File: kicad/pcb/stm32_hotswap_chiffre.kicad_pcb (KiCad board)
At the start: 2 copper layers, 227.4 x 84.9 mm, 119 parts, among them J1 USB_C_Receptacle_USB2.0, J2 SAM, J3 nRF52, J4 Conn_01x02_Socket, J5 Conn_01x02_Socket, Q2 AO3401A, SW1 SW_Push, SW10 SW_Push, SW11 SW_Push, SW12 SW_Push, SW13 SW_Push, SW14 SW_Push, SW15 SW_Push, SW16 SW_Push, SW17 SW_Push, SW18 SW_Push, SW19 SW_Push, SW2 SW_Push, SW20 SW_Push, SW21 SW_Push, SW22 SW_Push, SW23 SW_Push, SW24 SW_Push, SW25 SW_Push, SW26 SW_Push, SW27 SW_Push, SW28 SW_Push, SW29 SW_Push, SW3 SW_Push, SW30 SW_Push, SW31 SW_Push, SW32 SW_Push, SW33 SW_Push, SW34 SW_Push, SW35 SW_Push, SW37 Reset, SW4 SW_Push, SW5 SW_Push, SW6 SW_Push, SW7 SW_Push, SW8 SW_Push, SW9 SW_Push, U2 PRTR5V0U2X, U3 XC6206PxxxMR-Regulator_Linear, U4 ATSAML21E18B-AUT, U5 BC805M, U6 MCP73832-2-OT, U7 74LVC1G08, U8 74LVC1G08, U9 74LVC1G08, Y2 32.768 kHz

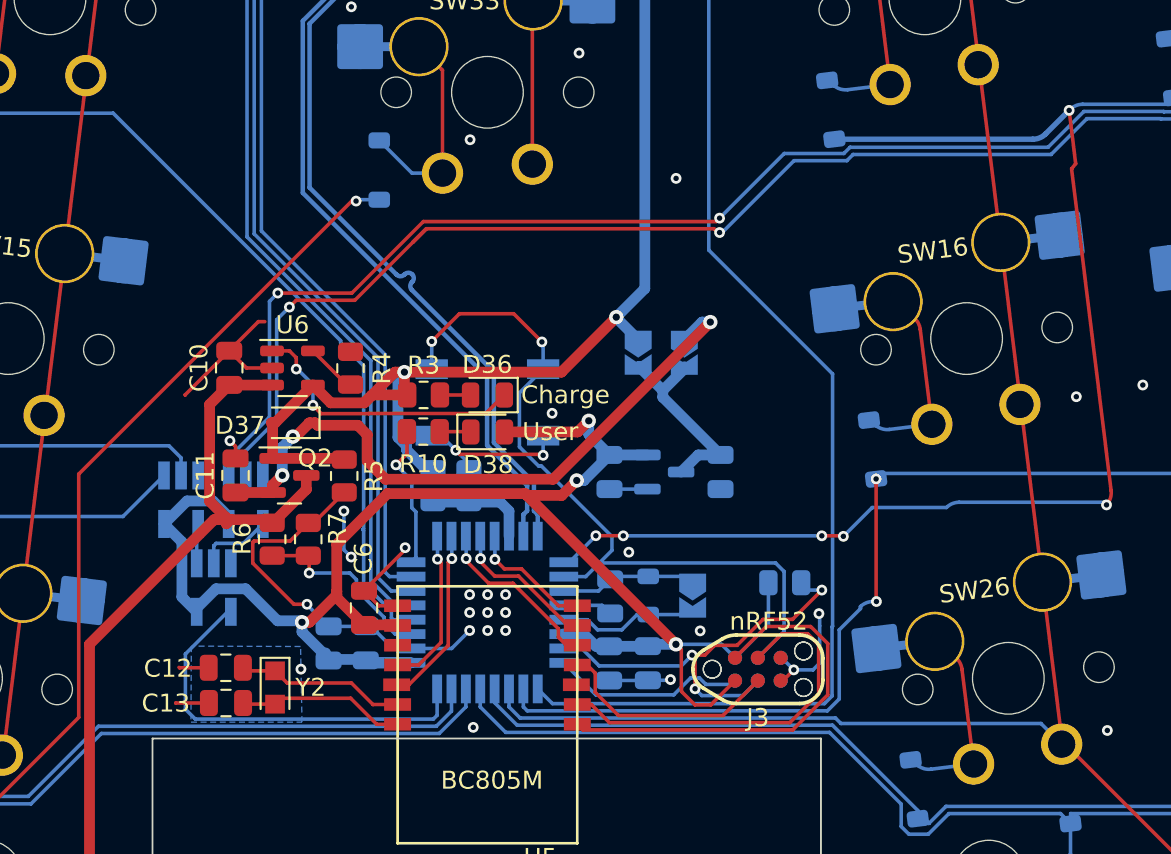
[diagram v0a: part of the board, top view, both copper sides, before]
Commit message: Rework pins to use proper wake/interrupt pins for all matrix outputs, fix edge cuts.
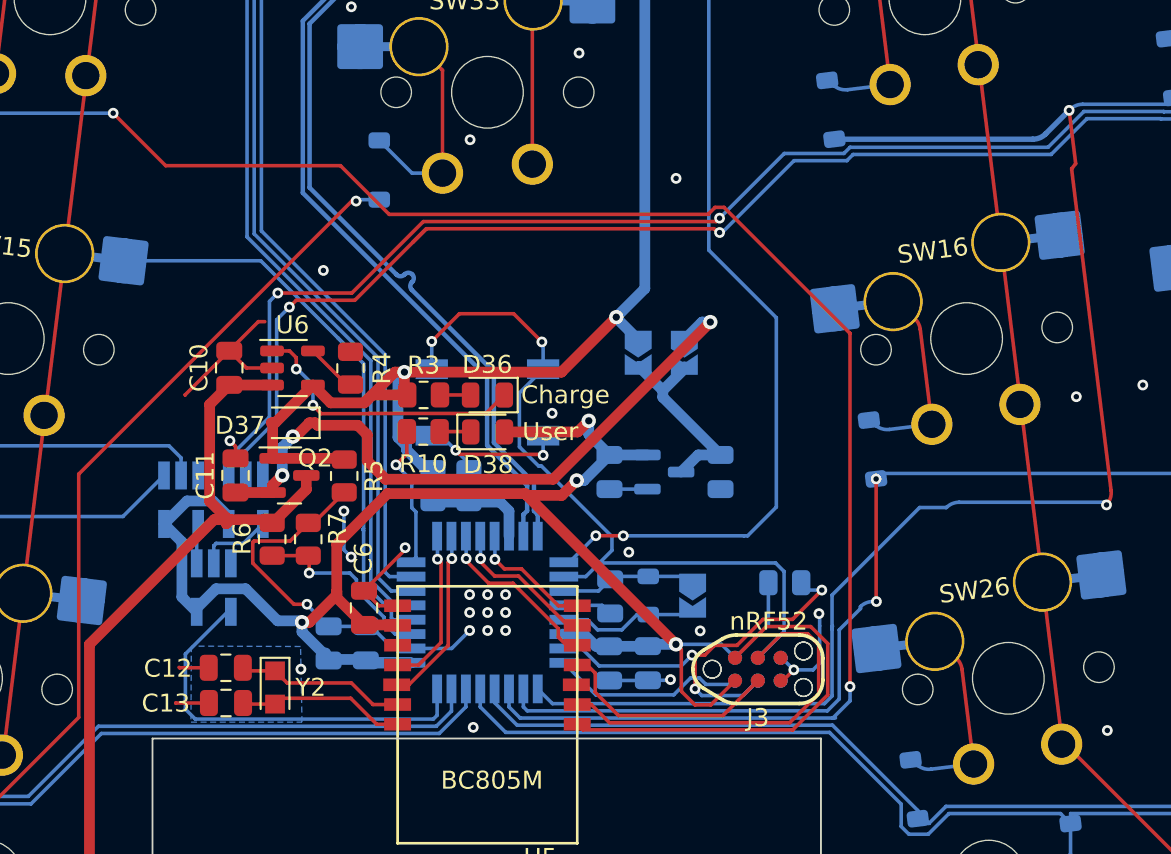
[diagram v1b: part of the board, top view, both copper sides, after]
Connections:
- U4 pad 1: col0 -> row0_r
- U4 pad 12: row0_l -> col4
- U4 pad 25: row0_r -> col0
- U4 pad 3: col4 -> row0_l
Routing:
- net row0_l: track 128.9 -> 180.8 mm, vias 0 -> 2
- net col0: track 425.5 -> 409.6 mm, vias 1 -> 3
- net row0_r: track 136.1 -> 144.9 mm, vias 6 -> 2
- net -BATT: vias 101 -> 102

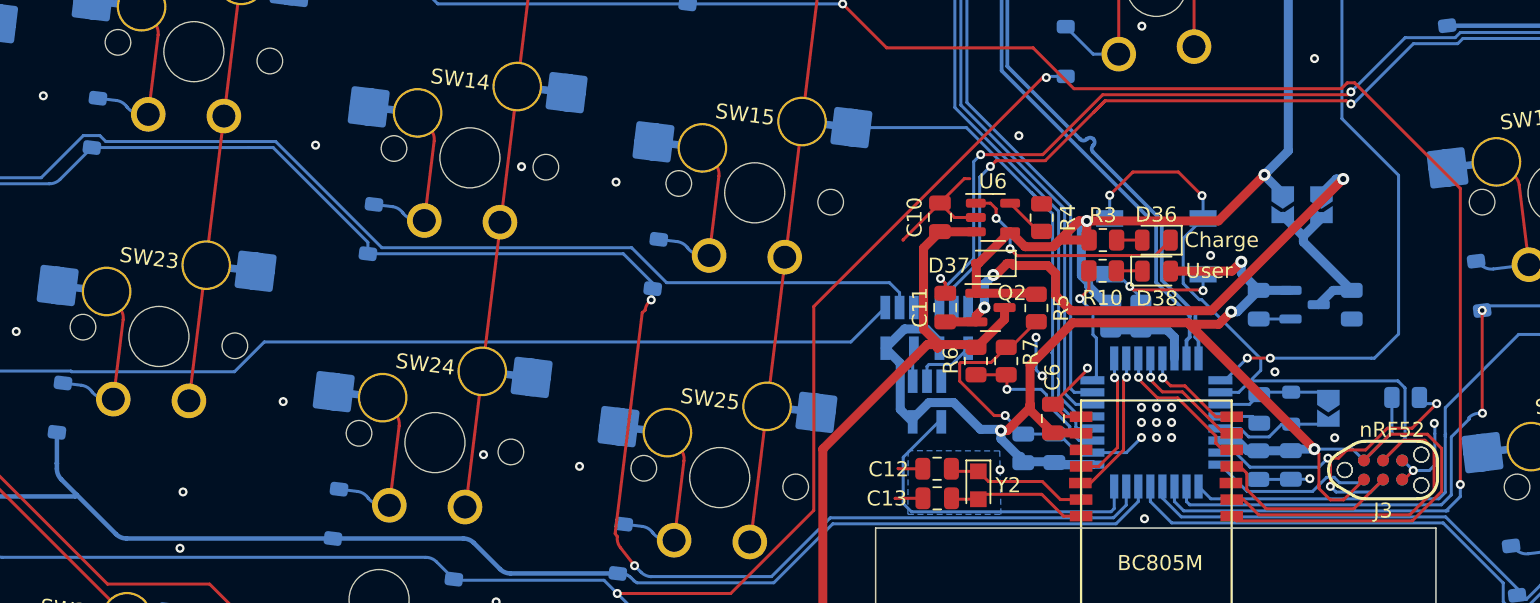
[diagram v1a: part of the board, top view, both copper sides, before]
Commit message: Minor cleanups of vias/traces and ERC happy.
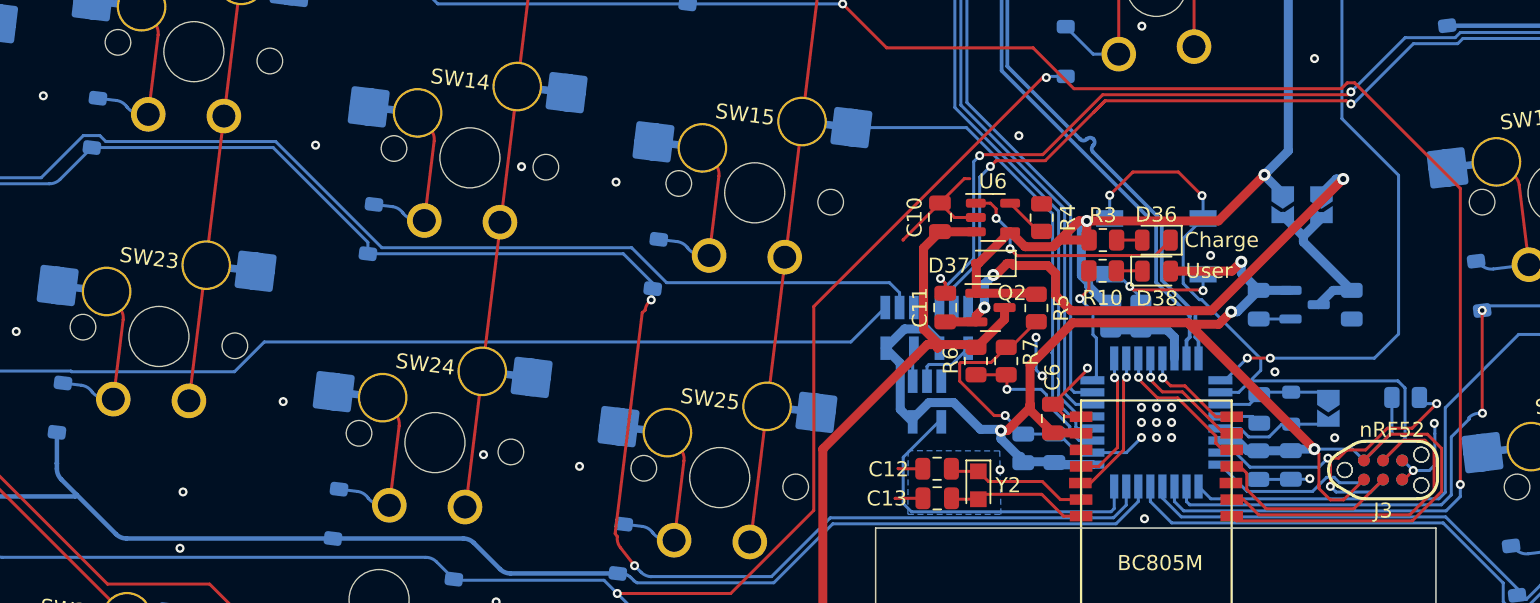
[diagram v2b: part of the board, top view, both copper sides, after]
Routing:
- net col4: track 200.1 -> 199.3 mm

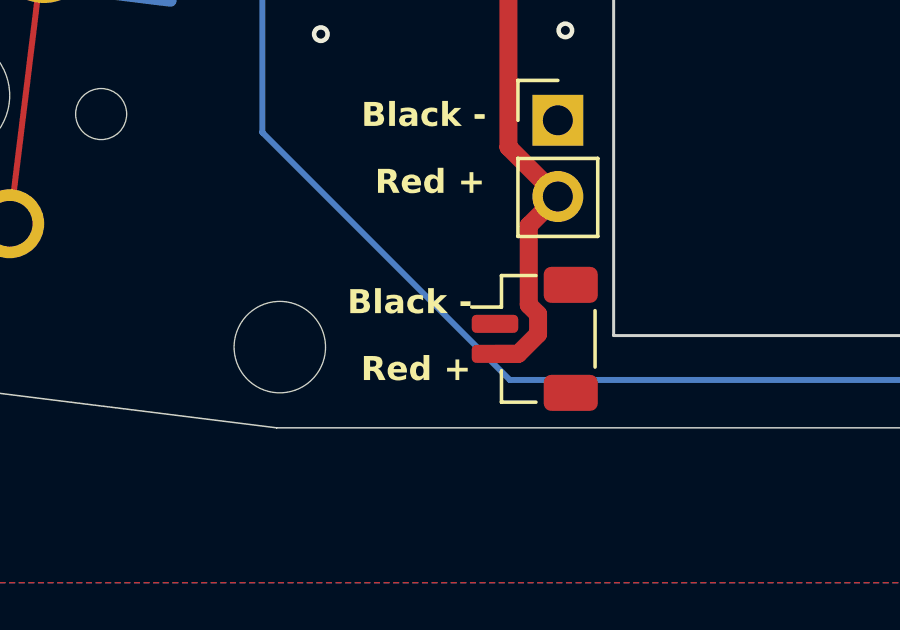
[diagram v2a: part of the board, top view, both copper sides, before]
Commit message: BOM tweaks, switch to horizontal JST SH.
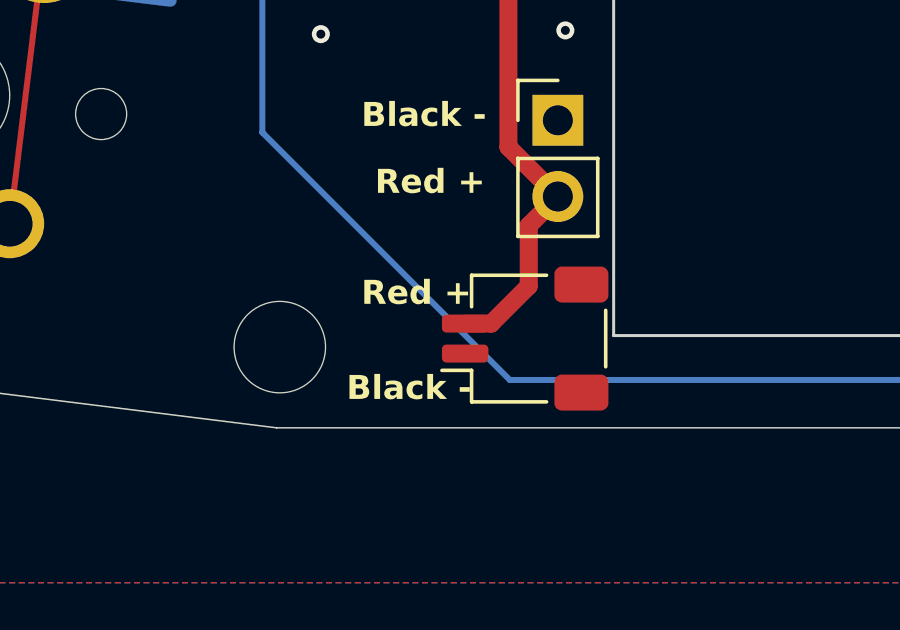
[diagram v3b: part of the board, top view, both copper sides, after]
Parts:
- J4: footprint Connector_JST:JST_SH_BM02B-SRSS-TB_1x02-1MP_P1.00mm_Vertical -> Connector_JST:JST_SH_SM02B-SRSS-TB_1x02-1MP_P1.00mm_Horizontal
- moved J4 0.32 mm to (125.0, 142.8), turned to 90 degrees
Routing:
- net +BATT: track 58.0 -> 57.2 mm
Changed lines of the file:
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@@
     )
   )
-  (footprint "Connector_JST:JST_SH_BM02B-SRSS-TB_1x02-1MP_P1.00mm_Vertical" (layer "F.Cu")
-    (at 125.369472 142.832513 -90)
-    (descr "JST SH series connector, BM02B-SRSS-TB (http://www.jst-mfg.com/product/pdf/eng/eSH.pdf), generated with kicad-footprint-generator")
-    (tags "connector JST SH side entry")
+  (footprint "Connector_JST:JST_SH_SM02B-SRSS-TB_1x02-1MP_P1.00mm_Horizontal" (layer "F.Cu")
+    (at 125.049472 142.822513 90)
+    (descr "JST SH series connector, SM02B-SRSS-TB (http://www.jst-mfg.com/product/pdf/eng/eSH.pdf), generated with kicad-footprint-generator")
+    (tags "connector JST SH top entry")
     (property "Sheetfile" "power.kicad_sch")
     (property "Sheetname" "power")
@@
     (property "ki_keywords" "connector")
     (attr smd)
-    (fp_text reference "J4" (at 0 -3.3 -270) (layer "F.SilkS") hide
+    (fp_text reference "J4" (at 0 -3.98 90) (layer "F.SilkS") hide
         (effects (font (size 1 1) (thickness 0.15)))
     )
-    (fp_text value "Conn_01x02_Socket" (at 0 3.3 -270) (layer "F.Fab")
+    (fp_text value "Conn_01x02_Socket" (at 0 3.98 90) (layer "F.Fab")
         (effects (font (size 1 1) (thickness 0.15)))
     )
-    (fp_text user "${REFERENCE}" (at 0 -0.25 -270) (layer "F.Fab")
+    (fp_text user "${REFERENCE}" (at 0 0 90) (layer "F.Fab")
         (effects (font (size 1 1) (thickness 0.15)))
     )
-    (fp_line (start -2.11 -0.04) (end -2.11 1.11)
+    (fp_line (start -2.11 -1.785) (end -1.06 -1.785)
       (stroke (width 0.12) (type solid)) (layer "F.SilkS"))
-    (fp_line (start -2.11 1.11) (end -1.06 1.11)
+    (fp_line (start -2.11 0.715) (end -2.11 -1.785)
       (stroke (width 0.12) (type solid)) (layer "F.SilkS"))
-    (fp_line (start -1.06 1.11) (end -1.06 2.1)
+    (fp_line (start -1.06 -1.785) (end -1.06 -2.775)
       (stroke (width 0.12) (type solid)) (layer "F.SilkS"))
-    (fp_line (start -0.94 -2.01) (end 0.94 -2.01)
+    (fp_line (start -0.94 2.685) (end 0.94 2.685)
       (stroke (width 0.12) (type solid)) (layer "F.SilkS"))
-    (fp_line (start 2.11 -0.04) (end 2.11 1.11)
+    (fp_line (start 2.11 -1.785) (end 1.06 -1.785)
       (stroke (width 0.12) (type solid)) (layer "F.SilkS"))
-    (fp_line (start 2.11 1.11) (end 1.06 1.11)
+    (fp_line (start 2.11 0.715) (end 2.11 -1.785)
       (stroke (width 0.12) (type solid)) (layer "F.SilkS"))
-    (fp_line (start -2.9 -2.6) (end -2.9 2.6)
+    (fp_line (start -2.9 -3.28) (end -2.9 3.28)
       (stroke (width 0.05) (type solid)) (layer "F.CrtYd"))
-    (fp_line (start -2.9 2.6) (end 2.9 2.6)
+    (fp_line (start -2.9 3.28) (end 2.9 3.28)
       (stroke (width 0.05) (type solid)) (layer "F.CrtYd"))
-    (fp_line (start 2.9 -2.6) (end -2.9 -2.6)
+    (fp_line (start 2.9 -3.28) (end -2.9 -3.28)
       (stroke (width 0.05) (type solid)) (layer "F.CrtYd"))
-    (fp_line (start 2.9 2.6) (end 2.9 -2.6)
+    (fp_line (start 2.9 3.28) (end 2.9 -3.28)
       (stroke (width 0.05) (type solid)) (layer "F.CrtYd"))
-    (fp_line (start -2 -1.9) (end 2 -1.9)
-      (stroke (width 0.1) (type solid)) (layer "F.Fab"))
-    (fp_line (start -2 1) (end -2 -1.9)
-      (stroke (width 0.1) (type solid)) (layer "F.Fab"))
-    (fp_line (start -2 1) (end 2 1)
-      (stroke (width 0.1) (type solid)) (layer "F.Fab"))
-    (fp_line (start -1 1) (end -0.5 0.292893)
-      (stroke (width 0.1) (type solid)) (layer "F.Fab"))
-    (fp_line (start -0.65 -1.55) (end -0.65 -0.95)
-      (stroke (width 0.1) (type solid)) (layer "F.Fab"))
-    (fp_line (start -0.65 -0.95) (end -0.35 -0.95)
-      (stroke (width 0.1) (type solid)) (layer "F.Fab"))
-    (fp_line (start -0.5 0.292893) (end 0 1)
-      (stroke (width 0.1) (type solid)) (layer "F.Fab"))
-    (fp_line (start -0.35 -1.55) (end -0.65 -1.55)
-      (stroke (width 0.1) (type solid)) (layer "F.Fab"))
-    (fp_line (start -0.35 -0.95) (end -0.35 -1.55)
+    (fp_line (start -2 -1.675) (end -2 2.575)
       (stroke (width 0.1) (type solid)) (layer "F.Fab"))
-    (fp_line (start 0.35 -1.55) (end 0.35 -0.95)
+    (fp_line (start -2 -1.675) (end 2 -1.675)
       (stroke (width 0.1) (type solid)) (layer "F.Fab"))
-    (fp_line (start 0.35 -0.95) (end 0.65 -0.95)
+    (fp_line (start -2 2.575) (end 2 2.575)
       (stroke (width 0.1) (type solid)) (layer "F.Fab"))
-    (fp_line (start 0.65 -1.55) (end 0.35 -1.55)
+    (fp_line (start -1 -1.675) (end -0.5 -0.967893)
       (stroke (width 0.1) (type solid)) (layer "F.Fab"))
-    (fp_line (start 0.65 -0.95) (end 0.65 -1.55)
+    (fp_line (start -0.5 -0.967893) (end 0 -1.675)
       (stroke (width 0.1) (type solid)) (layer "F.Fab"))
-    (fp_line (start 2 1) (end 2 -1.9)
+    (fp_line (start 2 -1.675) (end 2 2.575)
       (stroke (width 0.1) (type solid)) (layer "F.Fab"))
-    (pad "1" smd roundrect (at -0.5 1.325 270) (size 0.6 1.55) (layers "F.Cu" "F.Paste" "F.Mask") (roundrect_rratio 0.25)
+    (pad "1" smd roundrect (at -0.5 -2 90) (size 0.6 1.55) (layers "F.Cu" "F.Paste" "F.Mask") (roundrect_rratio 0.25)
       (net 81 "-BATT") (pinfunction "Pin_1") (pintype "passive"))
-    (pad "2" smd roundrect (at 0.5 1.325 270) (size 0.6 1.55) (layers "F.Cu" "F.Paste" "F.Mask") (roundrect_rratio 0.25)
+    (pad "2" smd roundrect (at 0.5 -2 90) (size 0.6 1.55) (layers "F.Cu" "F.Paste" "F.Mask") (roundrect_rratio 0.25)
       (net 76 "+BATT") (pinfunction "Pin_2") (pintype "passive"))
-    (pad "MP" smd roundrect (at -1.8 -1.2 270) (size 1.2 1.8) (layers "F.Cu" "F.Paste" "F.Mask") (roundrect_rratio 0.208333))
-    (pad "MP" smd roundrect (at 1.8 -1.2 270) (size 1.2 1.8) (layers "F.Cu" "F.Paste" "F.Mask") (roundrect_rratio 0.208333))
-    (model "${KICAD6_3DMODEL_DIR}/Connector_JST.3dshapes/JST_SH_BM02B-SRSS-TB_1x02-1MP_P1.00mm_Vertical.wrl"
+    (pad "MP" smd roundrect (at -1.8 1.875 90) (size 1.2 1.8) (layers "F.Cu" "F.Paste" "F.Mask") (roundrect_rratio 0.208333))
+    (pad "MP" smd roundrect (at 1.8 1.875 90) (size 1.2 1.8) (layers "F.Cu" "F.Paste" "F.Mask") (roundrect_rratio 0.208333))
+    (model "${KICAD6_3DMODEL_DIR}/Connector_JST.3dshapes/JST_SH_SM02B-SRSS-TB_1x02-1MP_P1.00mm_Horizontal.wrl"
       (offset (xyz 0 0 0))
       (scale (xyz 1 1 1))
@@
     (effects (font (size 0.8 0.8) (thickness 0.15) bold) (justify right bottom))
   )
-  (gr_text "Black -" (at 123.289472 142.072513) (layer "F.SilkS")
+  (gr_text "Red +" (at 123.264472 141.762513) (layer "F.SilkS")
     (effects (font (size 0.8 0.8) (thickness 0.15) bold) (justify right bottom))
   )
-  (gr_text "Red +" (at 123.249472 144.302513) (layer "F.SilkS")
+  (gr_text "Black -" (at 123.264472 144.932513) (layer "F.SilkS")
     (effects (font (size 0.8 0.8) (thickness 0.15) bold) (justify right bottom))
   )
@@
   (segment (start 156.399472 101.330013) (end 156.399472 100.947513) (width 0.6) (layer "B.Cu") (net 75))
   (segment (start 159.611972 104.542513) (end 156.399472 101.330013) (width 0.6) (layer "B.Cu") (net 75))
-  (segment (start 125.480678 142.011307) (end 125.169472 141.700101) (width 0.6) (layer "F.Cu") (net 76))
+  (segment (start 123.049472 142.322513) (end 123.919472 142.322513) (width 0.6) (layer "F.Cu") (net 76))
   (segment (start 124.492507 136.440548) (end 124.492507 115.079478) (width 0.6) (layer "F.Cu") (net 76))
   (segment (start 134.652419 108.372513) (end 136.559472 106.46546) (width 0.6) (layer "F.Cu") (net 76))
-  (segment (start 124.819471 143.332513) (end 125.480678 142.671306) (width 0.6) (layer "F.Cu") (net 76))
+  (segment (start 125.169472 141.072513) (end 125.169472 139.057513) (width 0.6) (layer "F.Cu") (net 76))
   (segment (start 131.179472 101.732512) (end 131.179472 107.112513) (width 0.6) (layer "F.Cu") (net 76))
   (segment (start 132.109472 108.042513) (end 132.109472 108.372512) (width 0.6) (layer "F.Cu") (net 76))
   (segment (start 126.139472 138.087513) (end 124.492507 136.440548) (width 0.6) (layer "F.Cu") (net 76))
   (segment (start 131.179472 107.112513) (end 132.109472 108.042513) (width 0.6) (layer "F.Cu") (net 76))
-  (segment (start 125.169472 141.700101) (end 125.169472 139.057513) (width 0.6) (layer "F.Cu") (net 76))
   (segment (start 131.429472 108.142513) (end 132.339472 108.142513) (width 0.6) (layer "F.Cu") (net 76))
-  (segment (start 125.480678 142.671306) (end 125.480678 142.011307) (width 0.6) (layer "F.Cu") (net 76))
   (segment (start 124.492507 115.079478) (end 131.429472 108.142513) (width 0.6) (layer "F.Cu") (net 76))
   (segment (start 132.339472 108.142513) (end 134.375365 108.142513) (width 0.6) (layer "F.Cu") (net 76))
   (segment (start 136.559472 106.46546) (end 136.559472 105.682513) (width 0.6) (layer "F.Cu") (net 76))
-  (segment (start 124.044472 143.332513) (end 124.819471 143.332513) (width 0.6) (layer "F.Cu") (net 76))
   (segment (start 132.269472 100.642513) (end 131.179472 101.732512) (width 0.6) (layer "F.Cu") (net 76))
+  (segment (start 123.919472 142.322513) (end 125.169472 141.072513) (width 0.6) (layer "F.Cu") (net 76))
   (segment (start 134.651972 100.652513) (end 132.279471 100.652512) (width 0.6) (layer "F.Cu") (net 76))
   (segment (start 125.169472 139.057513) (end 126.139472 138.087513) (width 0.6) (layer "F.Cu") (net 76))
